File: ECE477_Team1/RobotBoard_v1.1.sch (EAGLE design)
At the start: 86 parts, among them IC1L A3967SLB, IC1R A3967SLB, IC33 3.3, IC5 5

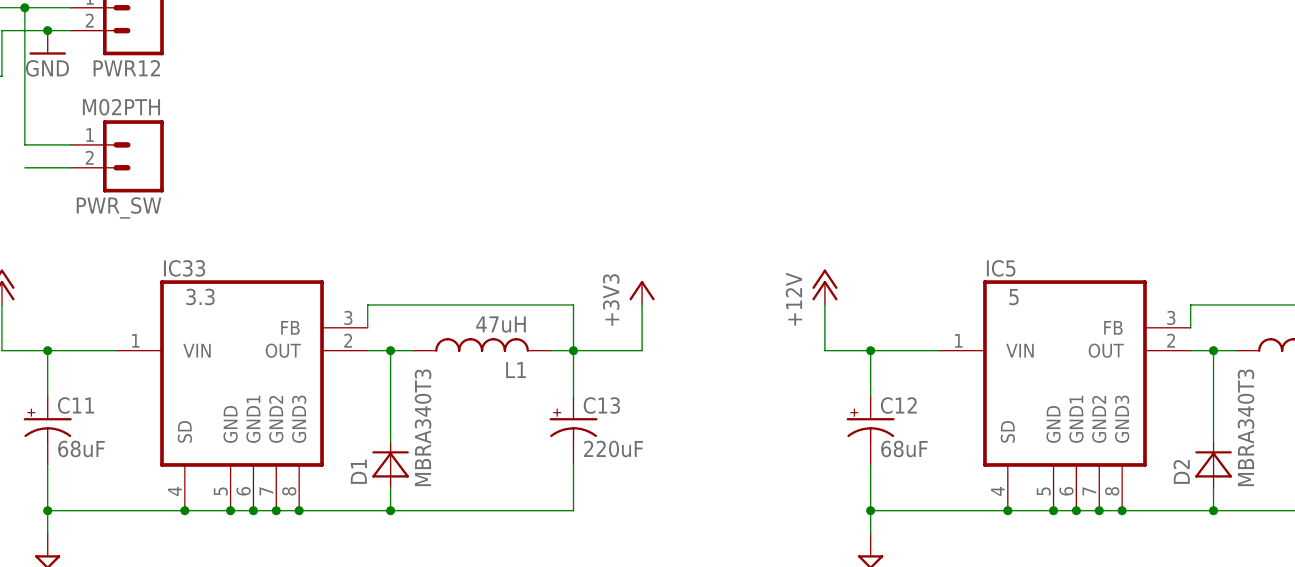
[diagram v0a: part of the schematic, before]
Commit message: Updated Power Regulators and created v2.0
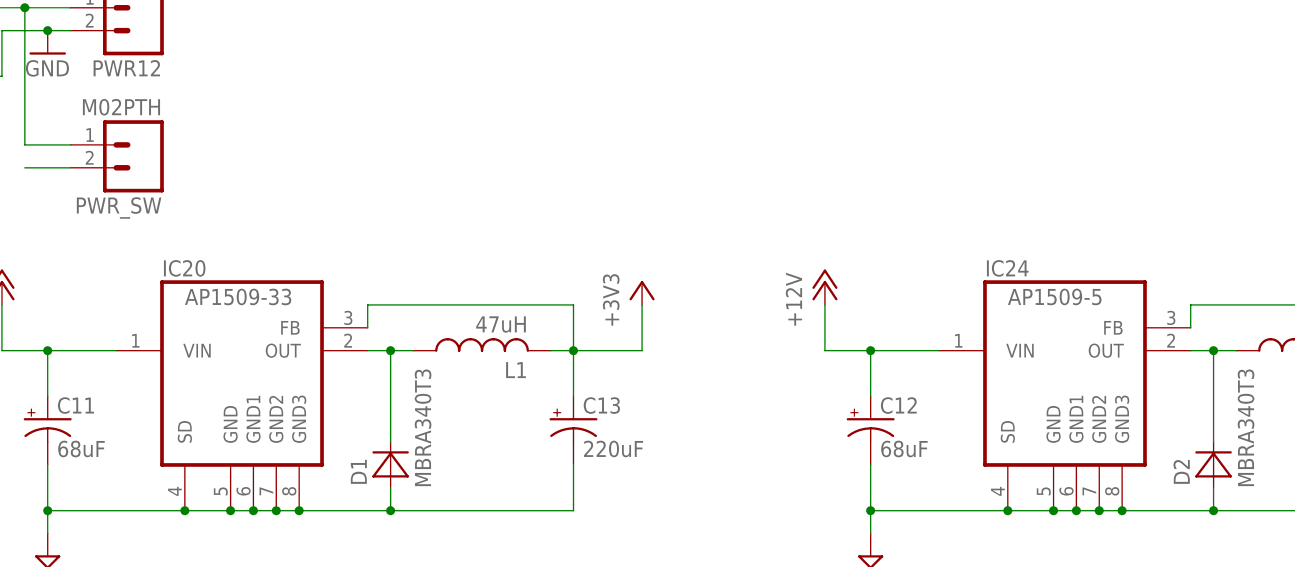
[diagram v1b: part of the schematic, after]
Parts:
- IC20: value 3.3 -> AP1509-33
- IC24: value 5 -> AP1509-5
- renumbered IC33 to IC20, IC5 to IC24
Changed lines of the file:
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@@
 <part name="R5" library="SparkFun03_30_09" deviceset="RESISTOR" device="0402" value="1K"/>
 <part name="ANT" library="Johanson_antenna" deviceset="2450AT18A100" device=""/>
-<part name="IC33" library="crw" deviceset="AP1509" device="" value="3.3"/>
+<part name="IC20" library="crw" deviceset="AP1509" device="" value="AP1509-33"/>
 <part name="P+4" library="supply1" deviceset="+12V" device=""/>
 <part name="D1" library="diode" deviceset="MBRA340T3" device=""/>
 <part name="+3V16" library="supply1" deviceset="+3V3" device=""/>
 <part name="SUPPLY37" library="supply2" deviceset="GND" device=""/>
-<part name="IC5" library="crw" deviceset="AP1509" device="" value="5"/>
+<part name="IC24" library="crw" deviceset="AP1509" device="" value="AP1509-5"/>
 <part name="P+16" library="supply1" deviceset="+12V" device=""/>
 <part name="D2" library="diode" deviceset="MBRA340T3" device=""/>
@@
 <instance part="R5" gate="G$1" x="-91.44" y="48.26" rot="R180"/>
 <instance part="ANT" gate="G$1" x="154.94" y="58.42"/>
-<instance part="IC33" gate="G$1" x="106.68" y="96.52"/>
+<instance part="IC20" gate="G$1" x="106.68" y="96.52"/>
 <instance part="P+4" gate="1" x="78.74" y="106.68"/>
 <instance part="D1" gate="G$1" x="121.92" y="86.36" rot="R90"/>
 <instance part="+3V16" gate="G$1" x="149.86" y="106.68"/>
 <instance part="SUPPLY37" gate="GND" x="83.82" y="76.2"/>
-<instance part="IC5" gate="G$1" x="198.12" y="96.52"/>
+<instance part="IC24" gate="G$1" x="198.12" y="96.52"/>
 <instance part="P+16" gate="1" x="170.18" y="106.68"/>
 <instance part="D2" gate="G$1" x="213.36" y="86.36" rot="R90"/>
@@
 <segment>
 <wire x1="83.82" y1="86.36" x2="83.82" y2="81.28" width="0.1524" layer="91"/>
-<pinref part="IC33" gate="G$1" pin="SD"/>
+<pinref part="IC20" gate="G$1" pin="SD"/>
 <wire x1="83.82" y1="81.28" x2="99.06" y2="81.28" width="0.1524" layer="91"/>
-<pinref part="IC33" gate="G$1" pin="GND3"/>
+<pinref part="IC20" gate="G$1" pin="GND3"/>
 <wire x1="99.06" y1="81.28" x2="104.14" y2="81.28" width="0.1524" layer="91"/>
 <wire x1="104.14" y1="81.28" x2="106.68" y2="81.28" width="0.1524" layer="91"/>
@@
 <junction x="121.92" y="81.28"/>
 <junction x="99.06" y="81.28"/>
-<pinref part="IC33" gate="G$1" pin="GND"/>
+<pinref part="IC20" gate="G$1" pin="GND"/>
 <junction x="104.14" y="81.28"/>
-<pinref part="IC33" gate="G$1" pin="GND1"/>
+<pinref part="IC20" gate="G$1" pin="GND1"/>
 <junction x="106.68" y="81.28"/>
-<pinref part="IC33" gate="G$1" pin="GND2"/>
+<pinref part="IC20" gate="G$1" pin="GND2"/>
 <junction x="109.22" y="81.28"/>
 <junction x="111.76" y="81.28"/>
@@
 <segment>
 <wire x1="175.26" y1="86.36" x2="175.26" y2="81.28" width="0.1524" layer="91"/>
-<pinref part="IC5" gate="G$1" pin="SD"/>
+<pinref part="IC24" gate="G$1" pin="SD"/>
 <wire x1="175.26" y1="81.28" x2="190.5" y2="81.28" width="0.1524" layer="91"/>
-<pinref part="IC5" gate="G$1" pin="GND3"/>
+<pinref part="IC24" gate="G$1" pin="GND3"/>
 <wire x1="190.5" y1="81.28" x2="195.58" y2="81.28" width="0.1524" layer="91"/>
 <wire x1="195.58" y1="81.28" x2="198.12" y2="81.28" width="0.1524" layer="91"/>
@@
 <wire x1="175.26" y1="81.28" x2="175.26" y2="78.74" width="0.1524" layer="91"/>
 <junction x="175.26" y="81.28"/>
-<pinref part="IC5" gate="G$1" pin="GND1"/>
+<pinref part="IC24" gate="G$1" pin="GND1"/>
 <junction x="198.12" y="81.28"/>
-<pinref part="IC5" gate="G$1" pin="GND2"/>
+<pinref part="IC24" gate="G$1" pin="GND2"/>
 <junction x="200.66" y="81.28"/>
-<pinref part="IC5" gate="G$1" pin="GND"/>
+<pinref part="IC24" gate="G$1" pin="GND"/>
 <junction x="195.58" y="81.28"/>
 <pinref part="C12" gate="G$1" pin="-"/>
@@
 <wire x1="149.86" y1="99.06" x2="149.86" y2="104.14" width="0.1524" layer="91"/>
 <wire x1="142.24" y1="99.06" x2="142.24" y2="104.14" width="0.1524" layer="91"/>
-<pinref part="IC33" gate="G$1" pin="FB"/>
+<pinref part="IC20" gate="G$1" pin="FB"/>
 <wire x1="142.24" y1="104.14" x2="119.38" y2="104.14" width="0.1524" layer="91"/>
 <wire x1="119.38" y1="104.14" x2="119.38" y2="101.6" width="0.1524" layer="91"/>
@@
 </segment>
 <segment>
-<pinref part="IC33" gate="G$1" pin="VIN"/>
+<pinref part="IC20" gate="G$1" pin="VIN"/>
 <wire x1="83.82" y1="99.06" x2="91.44" y2="99.06" width="0.1524" layer="91"/>
 <wire x1="83.82" y1="99.06" x2="83.82" y2="93.98" width="0.1524" layer="91"/>
@@
 </segment>
 <segment>
-<pinref part="IC5" gate="G$1" pin="VIN"/>
+<pinref part="IC24" gate="G$1" pin="VIN"/>
 <wire x1="175.26" y1="99.06" x2="182.88" y2="99.06" width="0.1524" layer="91"/>
 <wire x1="175.26" y1="99.06" x2="175.26" y2="93.98" width="0.1524" layer="91"/>
@@
 <wire x1="241.3" y1="99.06" x2="241.3" y2="104.14" width="0.1524" layer="91"/>
 <wire x1="233.68" y1="99.06" x2="233.68" y2="104.14" width="0.1524" layer="91"/>
-<pinref part="IC5" gate="G$1" pin="FB"/>
+<pinref part="IC24" gate="G$1" pin="FB"/>
 <wire x1="233.68" y1="104.14" x2="210.82" y2="104.14" width="0.1524" layer="91"/>
 <wire x1="210.82" y1="104.14" x2="210.82" y2="101.6" width="0.1524" layer="91"/>
@@
 <net name="N$40" class="0">
 <segment>
-<pinref part="IC33" gate="G$1" pin="OUT"/>
+<pinref part="IC20" gate="G$1" pin="OUT"/>
 <pinref part="D1" gate="G$1" pin="C"/>
 <wire x1="119.38" y1="99.06" x2="121.92" y2="99.06" width="0.1524" layer="91"/>
@@
 <net name="N$45" class="0">
 <segment>
-<pinref part="IC5" gate="G$1" pin="OUT"/>
+<pinref part="IC24" gate="G$1" pin="OUT"/>
 <pinref part="D2" gate="G$1" pin="C"/>
 <wire x1="210.82" y1="99.06" x2="213.36" y2="99.06" width="0.1524" layer="91"/>
